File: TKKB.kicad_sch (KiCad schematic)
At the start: 65 parts, among them J1 UP, J2 DOWN, J3 Power Connector, SW1 RESET, SW10 6, SW11 7, SW12 8, SW13 9, SW14 0, SW15 1, SW16 Q, SW17 W, SW18 E, SW19 R, SW2 REPEAT, SW20 T, SW21 Y, SW22 U, SW23 I, SW24 O, SW25 P, SW26 FIRE, SW27 FIRE, SW28 UP, SW29 DOWN, SW3 SPACE, SW30 RETURN, SW31 CTRL, SW32 A, SW33 S, SW34 D, SW35 F, SW36 G, SW37 H, SW38 J, SW39 K, SW4 SPACE, SW40 L, SW41 :, SW42 LEFT, SW43 RIGHT, SW44 SHIFT, SW45 SHIFT, SW46 Z, SW47 X, SW48 C, SW49 V, SW5 SPACE, SW50 B, SW51 N, SW52 M, SW53 ,, SW54 ., SW55 ?, SW6 2, SW7 3, SW8 4, SW9 5

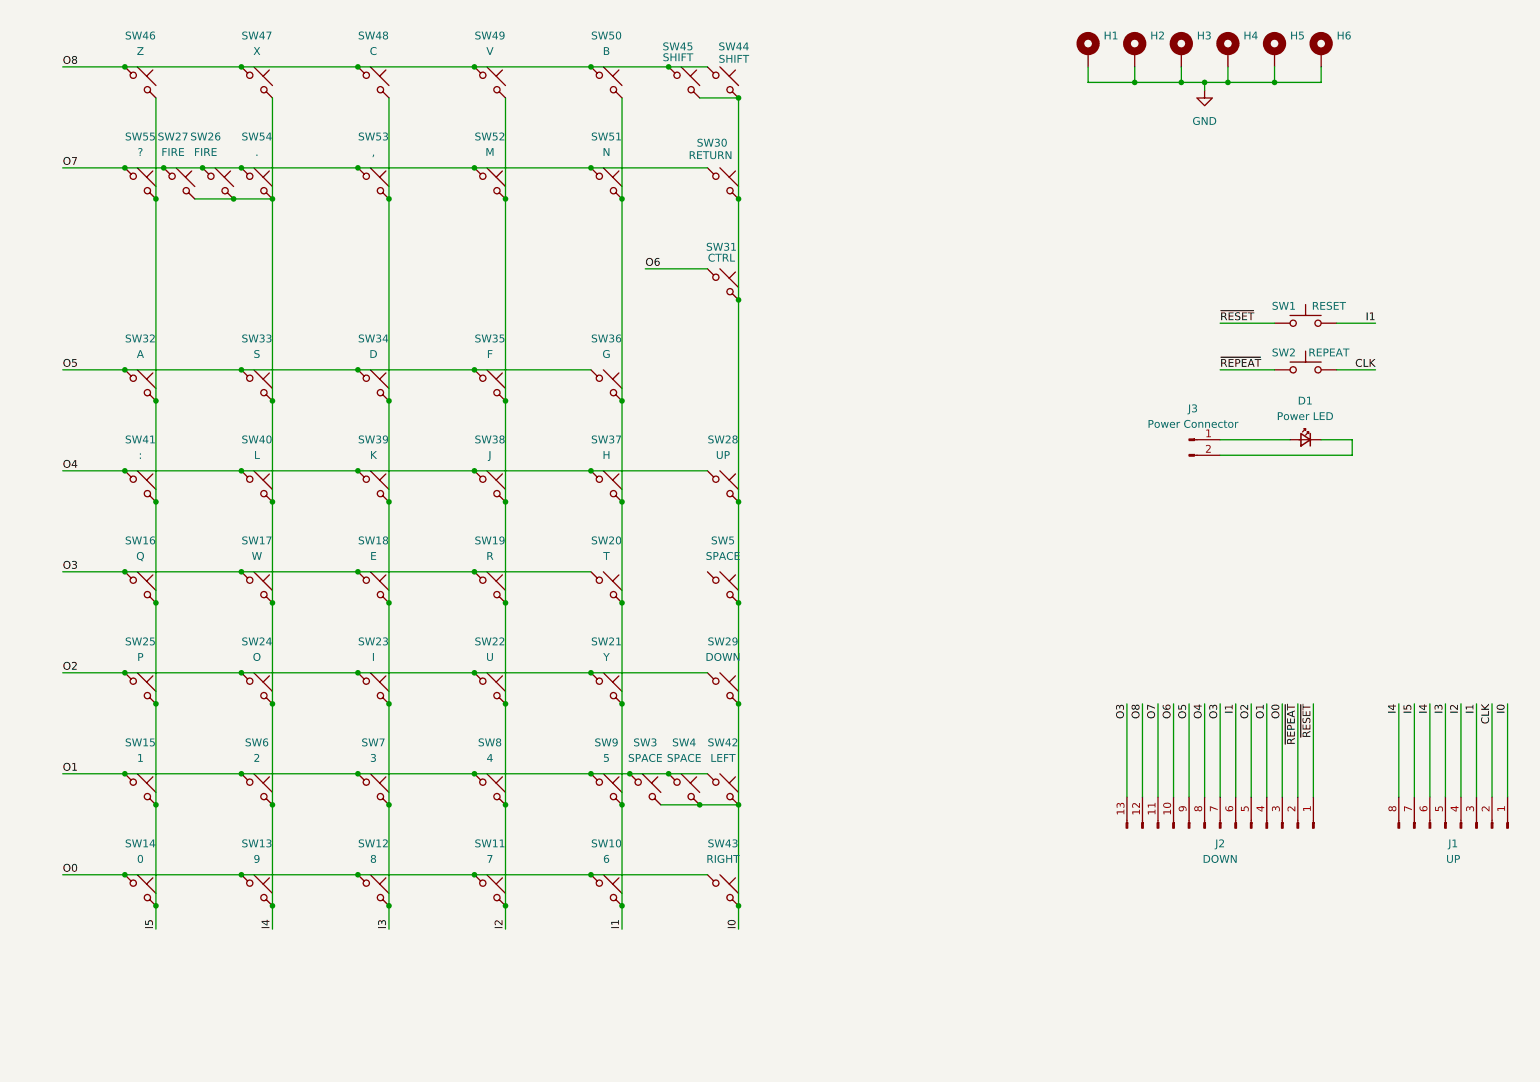
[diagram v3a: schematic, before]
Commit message: Created the base keyboard
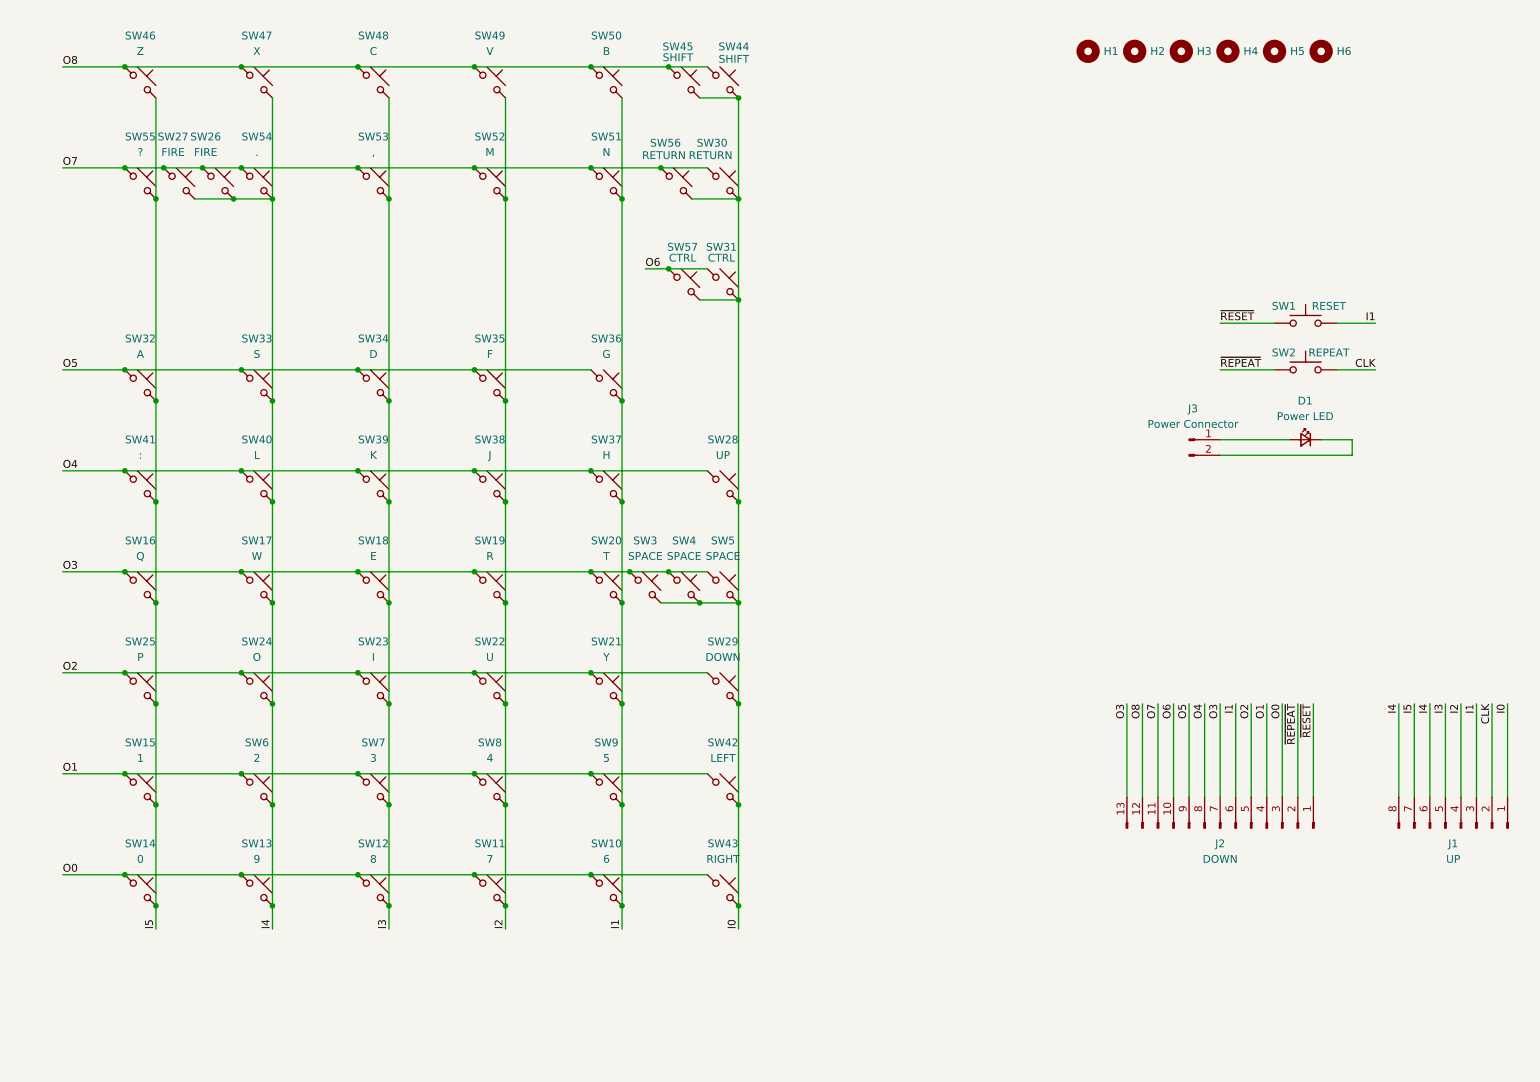
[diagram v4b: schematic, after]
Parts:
- added SW56: RETURN, buttons:SW_Push_SMD_Large, symbol Switch:SW_Push_45deg
- added SW57: CTRL, buttons:SW_Push_SMD_Large, symbol Switch:SW_Push_45deg
- H1, H2, H3, H4, H5, H6: footprint MountingHole:MountingHole_3.2mm_M3_Pad -> MountingHole:MountingHole_3.2mm_M3_ISO7380; symbol Mechanical:MountingHole_Pad -> Mechanical:MountingHole
- J1: footprint Connector_PinHeader_2.54mm:PinHeader_1x08_P2.54mm_Horizontal -> Connector_PinHeader_2.54mm:PinHeader_1x08_P2.54mm_Vertical
- J2: footprint Connector_PinHeader_2.54mm:PinHeader_1x13_P2.54mm_Horizontal -> Connector_PinHeader_2.54mm:PinHeader_1x13_P2.54mm_Vertical
- J3: footprint Connector_PinHeader_2.54mm:PinHeader_1x02_P2.54mm_Horizontal -> Connector_PinHeader_2.54mm:PinHeader_1x02_P2.54mm_Vertical
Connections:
- net I0: now also SW56.2, SW57.2
- net O1: no longer SW3.1, SW4.1
- net O3: now also SW3.1, SW4.1, SW5.1
- net O6: now also SW57.1
- net O7: now also SW56.1
- removed net GND: H1.1, H2.1, H3.1, H4.1, H5.1, H6.1
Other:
- moved on the sheet: SW3, SW4

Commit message: Add silkscreen for every key
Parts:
- D1: footprint LED_SMD:LED_1206_3216Metric_Pad1.42x1.75mm_HandSolder -> LED_THT:LED_D3.0mm
- SW41: value : -> : ;
- SW53: value , -> , <
- SW54: value . -> . >
- SW55: value ? -> ? /
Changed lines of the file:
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@@
 			)
 		)
-		(property "Value" "?"
+		(property "Value" "?   /"
 			(at 39.37 44.45 0)
 			(effects
@@
 			)
 		)
-		(property "Value" ":"
+		(property "Value" ":   ;"
 			(at 39.37 93.98 0)
 			(effects
@@
 			)
 		)
-		(property "Value" "."
+		(property "Value" ".   >"
 			(at 58.42 44.45 0)
 			(effects
@@
 			)
 		)
-		(property "Value" ","
+		(property "Value" ",   <"
 			(at 77.47 44.45 0)
 			(effects
@@
 			)
 		)
-		(property "Footprint" "LED_SMD:LED_1206_3216Metric_Pad1.42x1.75mm_HandSolder"
+		(property "Footprint" "LED_THT:LED_D3.0mm"
 			(at 229.87 91.44 90)
 			(effects

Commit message: Add more stand holes for the keyboard
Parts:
- added H10, H7, H8, H9: MountingHole_Pad, MountingHole:MountingHole_3.2mm_M3_ISO7380, symbol Mechanical:MountingHole
